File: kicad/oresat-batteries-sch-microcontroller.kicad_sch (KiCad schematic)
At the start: 28 parts, among them J2 SM14B-SHLS-TF, U20 TCAN330, U21 STM32F091C, X3 ECS-160-10-36Q-ES-TR

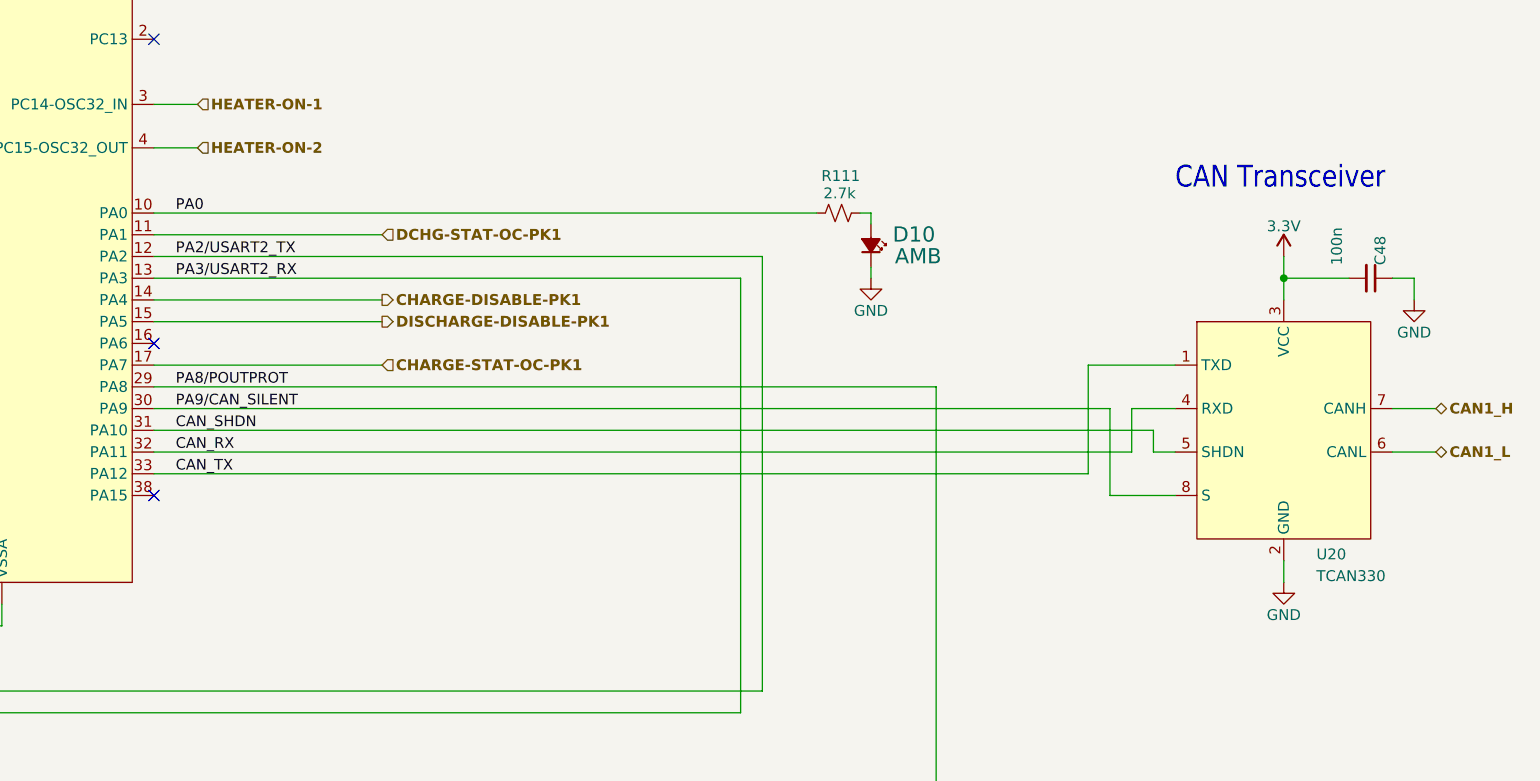
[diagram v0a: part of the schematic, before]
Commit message: Updated BOM, ready for polish and switch to MCXN
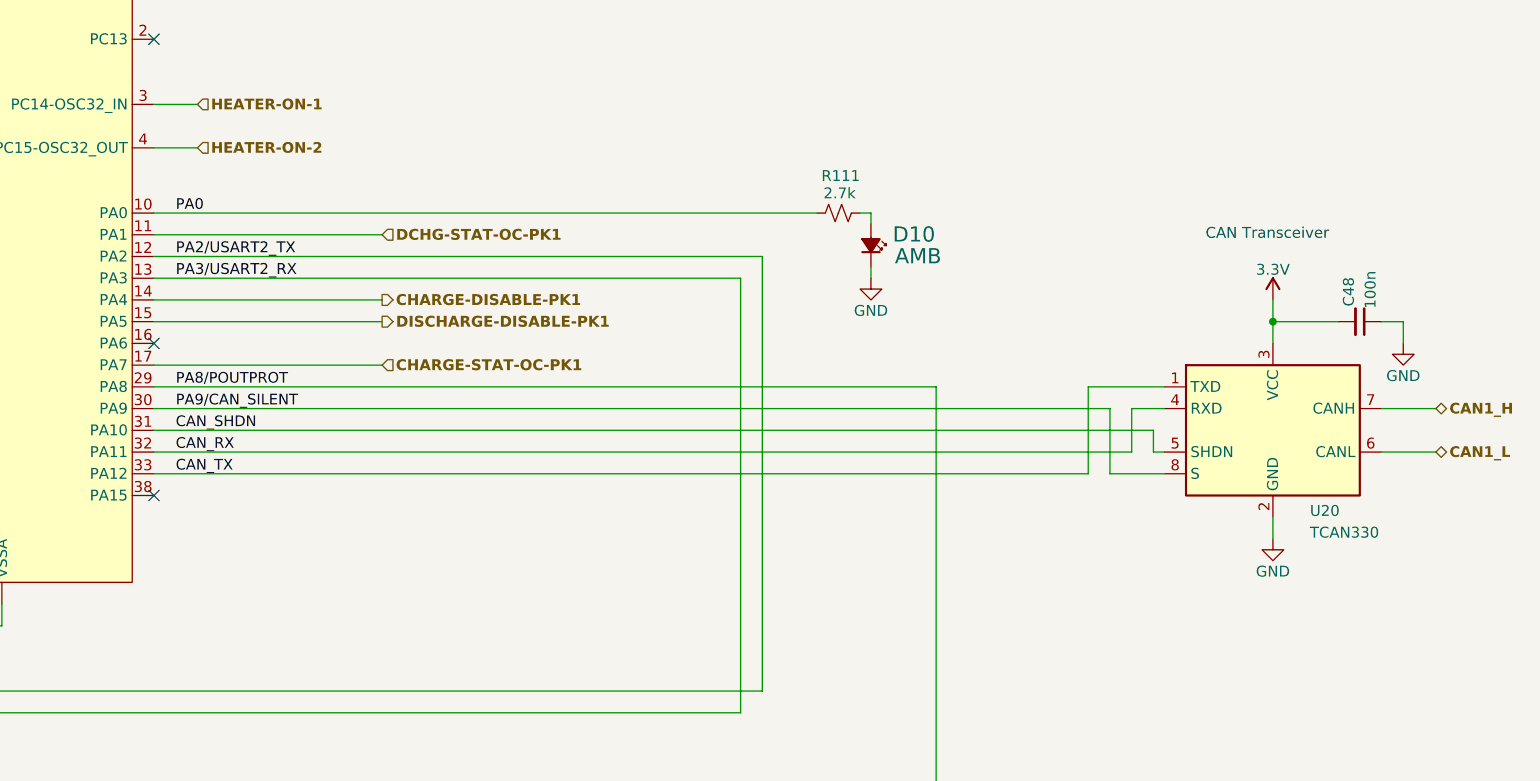
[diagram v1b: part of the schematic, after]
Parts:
- U20: footprint oresat-batteries:SOT23-8_TI-DCN -> Package_TO_SOT_SMD:SOT-23-8; symbol oresat-batteries-eagle-import:TCAN330 -> Interface_CAN_LIN:TCAN330
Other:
- moved on the sheet: C48, U20

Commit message: Not sure what changed from back in February, but committing anyway :)
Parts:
- C44, C45, C48, C49, C50: DIS Digi-Key -> DigiKey; DPN 399-1099-1-ND -> 399-6856-1-ND; MFR Samsung -> KEMET; MPN C0603C104M4RACTU -> C0603C104K5RACAUTO
- D10: DIS Digi-Key -> DigiKey; DPN 1830-1064-1-ND -> 732-150060AS75000CT-ND; MFR Inolux -> Wurth; MPN IN-S63AT5A -> 150060AS75000
- R110, R112: DIS Digi-Key -> DigiKey; DPN 311-10.0KHRCT-ND -> RMCF0603FT10K0CT-ND; MFR Yageo -> Stackpole Electronics; MPN RC0603FR-0710KL -> RMCF0603FT10K0
- R111: DIS Digi-Key -> DigiKey; DPN A129693CT-ND -> RMCF0603FT2K70CT-ND; MFR TE -> Stackpole Electronics; MPN CRGCQ0603F2K7 -> RMCF0603FT2K70
- R113, R114, R63, R64: DIS Digi-Key -> DigiKey; DPN RR08P4.7KDCT-ND -> RMCF0603FT4K70CT-ND; MFR TE Connectivity -> Stackpole Electronics; MPN RR0816P-472-D -> RMCF0603FT4K70
- R68, R72: DIS Digi-Key -> DigiKey; DPN RR08P4.7KDCT-ND -> RMCF0603FT10K0CT-ND; MFR TE Connectivity -> Stackpole Electronics; MPN RR0816P-472-D -> RMCF0603FT10K0
- U20: value TCAN330 -> TCAN330G; symbol Interface_CAN_LIN:TCAN330 -> Interface_CAN_LIN:TCAN330G; DIS Digi-Key -> DigiKey
- U21: DIS Digi-Key -> DigiKey; MPN STM32F091CBT6 -> STM32F091CCT7
- X3: DIS Digi-Key -> DigiKey

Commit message: Updated data, spiffed up the root page, renamed some STM specific OPD signals, synced SCH and BRD, fixed a bunch of DRC errors, NOW ready for MCXN import that will screw everything up.
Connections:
- net PA2/USART2_TX renamed MCU-UART-TX
- net PA3/USART2_RX renamed MCU-UART-RX
- net PB6/SCL renamed I2C1_SCL
- net PB7/SDA renamed I2C1_SDA
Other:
- note removed: "Emergency M0 bootstrapping over OPD I2C Address: 0b0111110x"
- note removed: "NOTE: PB6 and PB7 tied together via 2x 10k resistors @ MAX7310~{}"
- moved on the sheet: R110, R113, R114, TP21, TP22, TP78

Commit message: Added MCXN. Preliminary power layout, started removal of old symbols and footprints.
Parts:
- removed C46, C47: 20p, oresat-passives:0603-C-NOSILK, symbol Device:C_Small
- removed C49, C50: 100n, oresat-passives:0603-C-NOSILK, symbol Device:C_Small
- removed R110, R112, R68, R72: 10k, oresat-passives:0603-C-NOSILK, symbol Device:R_Small_US
- removed TP34, TP78, TP83: TEST-POINT-LARGE-SQUARE, oresat-misc:TestPoint-0.75mm-th, symbol oresat-misc:Test-Point-0.75mm-th
- removed U21: STM32F091C, oresat-batteries:STM32F091C, symbol oresat-batteries-eagle-import:STM32F091C
- removed X3: ECS-160-10-36Q-ES-TR, oresat-batteries:CRYSTAL_2.5X2, symbol oresat-batteries-eagle-import:CRYSTAL-WITH-GND
- added C38, C39: 4.7p, oresat-passives:0603-C-NOSILK, symbol Device:C_Small
- added C40, C52, C54, C55, C56, C57, C58, C59, C60: 100n, oresat-passives:0603-C-NOSILK, symbol Device:C_Small
- added C41: 1u, oresat-passives:0603-C-NOSILK, symbol Device:C_Small
- added C42: 2.2u, oresat-passives:0603-C-NOSILK, symbol Device:C_Small
- added C43: 22u, oresat-passives:0603-C-NOSILK, symbol Device:C_Small
- added C51, C53: 4.7u, oresat-passives:0603-C-NOSILK, symbol Device:C_Small
- added FB1: 120 ohm, oresat-passives:0805-B-NOSILK, symbol Device:FerriteBead_Small
- added L3: 1.5u, Inductor_SMD:L_0805_2012Metric, symbol Device:L_Small
- added R102: 1k, oresat-passives:0603-C-NOSILK, symbol Device:R_US
- added R108: 10k, oresat-passives:0603-C-NOSILK, symbol Device:R_Small_US
- added R115: 10k, oresat-passives:0603-C-NOSILK, symbol Device:R_US
- added TP113, TP6: Test-Point, oresat-misc:TestPoint-0.75mm-th, symbol oresat-misc:Test-Point-0.75mm-th
- added U7: MCXN947VKLT, oresat-ics:MCXN947KVLT-QFP50P1600X1600X160-101N, symbol oresat-ics:MCXN947VKLT
- added Y2: 24 MHz, Crystal:Crystal_SMD_2016-4Pin_2.0x1.6mm, symbol Device:Crystal_GND24_Small
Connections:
- net ALERTA-PK1: now also U7.22 (P4_0/ANA_0)
- net ALERTA-PK2: now also U7.28 (P4_6/ANA_6)
- net CHARGE-DISABLE-PK1: now also U7.25 (P4_3)
- net CHARGE-DISABLE-PK2: now also U7.36 (P4_13/ANA_14)
- net CHARGE-STAT-OC-PK1: now also U7.23 (P4_1/ANA_1)
- net CHARGE-STAT-OC-PK2: now also U7.29 (P4_7/ANA_7)
- net DCHG-STAT-OC-PK1: now also U7.24 (P4_2)
- net DCHG-STAT-OC-PK2: now also U7.35 (P4_12)
- net DISCHARGE-DISABLE-PK1: now also U7.26 (P4_4/ANA_4)
- net DISCHARGE-DISABLE-PK2: now also U7.37 (P4_15)
- net GND: now also C44.2, C45.2, C38.2, C39.2, C40.2, C41.2, C42.2, C43.2, C51.2, C52.2, C53.2, C54.2, C55.2, C56.2, C57.2, C58.2, C59.2, C60.2, U7.101 (EP), U7.32 (VREFL), U7.33 (VSS_P4), U7.52 (VSS_DCDC), Y2.2 (G), Y2.4 (G); no longer C44.1, C45.1
- net HEATER-ON-1: now also U7.27 (P4_5/ANA_5)
- net HEATER-ON-2: now also U7.38 (P4_16)
- net I2C1_SCL: now also U7.85 (P0_17)
- net I2C1_SDA: now also U7.84 (P0_16)
- net I2C2_SCL: now also R64.1, TP20.1, U7.93 (P1_1); no longer R63.1, TP19.1
- net I2C2_SDA: now also R63.1, TP19.1, U7.92 (P1_0); no longer R64.1, TP20.1
- net MCU-UART-RX: now also U7.1 (P1_8)
- net MCU-UART-TX: now also U7.2 (P1_9)
- net MOARPWR: now also U7.39 (P4_17/ANA_18)
- net SWCLK: now also U7.77 (P0_1)
- net SWDIO: now also U7.76 (P0_0)
- net at J2.8 (DEBUG-0): now also TP6.1
- net SWO: now reaches J2.13 (SWO)
- net SWO: now also U7.78 (P0_2)
- net 3.3V renamed +3.3V
- net +3.3V: now also C44.1, C45.1, C40.1, C51.1, C52.1, C54.1, C56.1, C57.1, C58.1, C59.1, FB1.1, R108.2, R115.2, U7.13 (VDD_LDO_CORE/VDD/VDD_P2), U7.34 (VDD_P4), U7.44 (VDD_USB), U7.47 (VDD_BAT), U7.54 (VDD_DCDC/VDD_LDO_SYS), U7.59 (VDD_P3), U7.66 (VDD_P3), U7.73 (VDD_P3), U7.83 (VDD), U7.96 (VDD); no longer C44.2, C45.2
- net CAN_RX: no longer names the net of U20.4 (RXD)
- net CAN_RX: now also U7.4 (P1_11)
- net CAN_SHDN: no longer names the net of U20.5 (SHDN)
- net CAN_TX: no longer names the net of U20.1 (TXD)
- net CAN_TX: now also U7.3 (P1_10)
- net NRESET renamed RESET
- net RESET: now also C60.1, R108.1, TP113.1, U7.9 (RESET_B)
- net PA0: no longer names the net of R111.2
- net PA0: now also U7.6 (P1_13)
- net PA9/CAN_SILENT: no longer names the net of U20.8 (S)
- new net: C38.1, U7.11 (P1_31), Y2.1
- new net: C39.1, U7.10 (P1_30), Y2.3
- new net: L3.2, U7.53 (DCDC_LX)
- new net 411-IOUT: R102.2
- new net P0_18: U7.86 (P0_18)
- new net P0_19: U7.87 (P0_19)
- new net P0_20: U7.88 (P0_20)
- new net P0_21: U7.89 (P0_21)
- new net P0_22: U7.90 (P0_22)
- new net P0_23: U7.91 (P0_23)
- new net P0_4: U7.80 (P0_4)
- new net P0_5: U7.81 (P0_5)
- new net P1_12: U7.5 (P1_12)
- new net P1_14: U7.7 (P1_14)
- new net P1_15: U7.8 (P1_15)
- new net P1_2: U7.94 (P1_2)
- new net P1_3: U7.95 (P1_3)
- new net P1_4: U7.97 (P1_4)
- new net P1_5: U7.98 (P1_5)
- new net P1_6: U7.99 (P1_6)
- new net P1_7: U7.100 (P1_7)
- new net P2_0: U7.14 (P2_0)
- new net P2_1: U7.15 (P2_1)
- new net P2_2: U7.16 (P2_2)
- new net P2_3: U7.17 (P2_3)
- new net P2_4: U7.18 (P2_4)
- new net P2_5: U7.19 (P2_5)
- new net P2_6: U7.20 (P2_6)
- new net P2_7: U7.21 (P2_7)
- new net P3_0: U7.75 (P3_0)
- new net P3_1: U7.74 (P3_1)
- new net P3_10: U7.68 (P3_10)
- new net P3_11: U7.67 (P3_11)
- new net P3_12: U7.65 (P3_12)
- new net P3_13: U7.64 (P3_13)
- new net P3_14: U7.63 (P3_14)
- new net P3_15: U7.62 (P3_15)
- new net P3_16: U7.61 (P3_16)
- new net P3_17: U7.60 (P3_17)
- new net P3_20: U7.57 (P3_20)
- new net P3_21: U7.56 (P3_21)
- new net P3_6: U7.72 (P3_6)
- new net P3_7: U7.71 (P3_7)
- new net P3_8: U7.70 (P3_8)
- new net P3_9: U7.69 (P3_9)
- new net P4_19: U7.40 (P4_19)
- new net P4_20: U7.41 (P4_20)
- new net P4_21: R102.1, U7.42 (P4_21/ANA_22)
- new net P4_23: U7.43 (P4_23)
- new net P5_0: U7.48 (P5_0)
- new net P5_1: U7.49 (P5_1)
- new net P5_2: U7.50 (P5_2)
- new net P5_3: U7.51 (P5_3)
- new net TDI : U7.79 (P0_3)
- new net VDD_ANA: C41.1, FB1.2, U7.30 (VDD_ANA), U7.31 (VREFH)
- new net VDD_CORE: C43.1, C53.1, C55.1, L3.1, U7.12 (VDD_CORE), U7.58 (VDD_CORE)
- new net VDD_SYS: C42.1, U7.55 (VDD_SYS)
- new net ~{ISPMODE}: R115.1, U7.82 (P0_6)
- no-connect marks 8 -> 55
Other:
- note added: "1.0 - 1.2 V depending on Active mode"
- note added: "24 MHz allows LPTMRs to work"
- note added: "4V"
- note added: "Note: Disable LDO_CORE in software for more power savings"
- note added: "OreSat Debug Connector"
- note added: "P0/P1"
- note added: "RX-TX cross on DEBUG board"
- note added: "VDD_BAT"
- note removed: "Battery CAN ID (SW pullups~{})"
- note removed: "Each VDD pin bypassed"
- note removed: "NRST pull-up built in"
- note removed: "Power/Current draw from OPD. Signal is analog voltage 0-1.2V"
- note removed: "Rx-Tx switch happens on programming board"
- note removed: "VBAT not bypassed becase not enough room instead tied into nearest bypass cap"
- moved on the sheet: C48, D10, J2, R111, R113, R114, R63, R64, TP19, TP20, TP21, TP22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

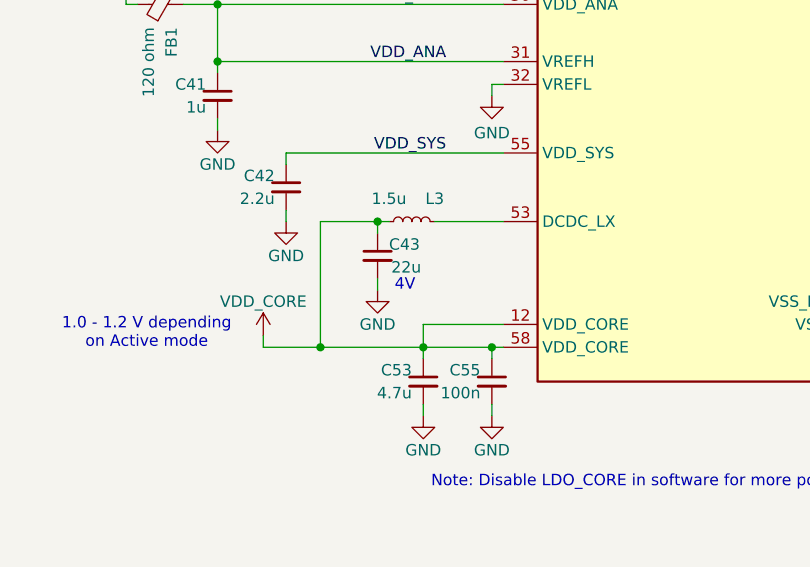
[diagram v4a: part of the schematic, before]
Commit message: Intermediary state on v4. Added one of two efuses.
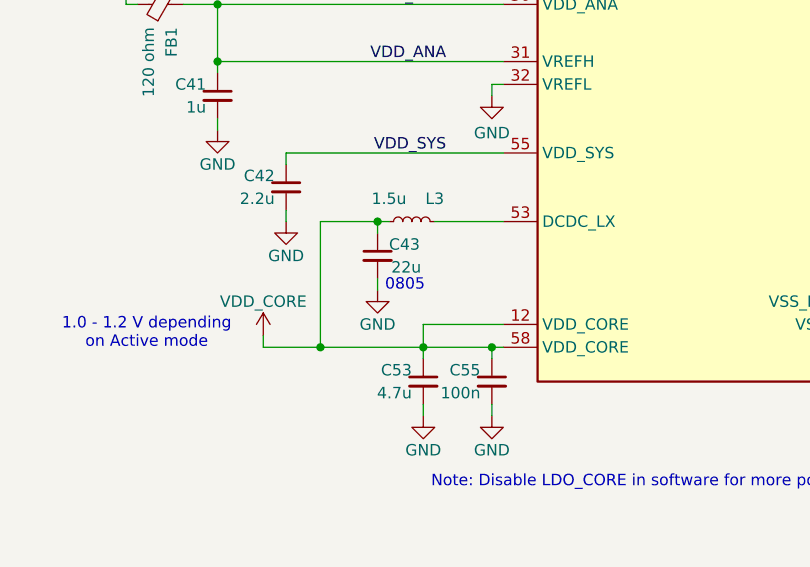
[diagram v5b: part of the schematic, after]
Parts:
- C43: footprint oresat-passives:0603-C-NOSILK -> oresat-passives:0805-C-NOSILK; DPN 478-KAM15CT70G226KTCT-ND -> 490-GRT21BC81C226ME13LCT-ND; MFR KYOCERA AVX -> Murata Electronics; MPN KAM15CT70G226KT -> GRT21BC81C226ME13L
- C51, C53: DPN 587-4332-1-ND -> 490-GRT188C71C475KE13DCT-ND; MFR Taiyo Yuden -> Murata Electronics; MPN EMK107BBJ475KAHT -> GRT188C71C475KE13D
- R102: DPN RMCF0603FT1K00CT-ND -> RMCF0603FT2K70CT-ND; MFR Stackpole Electronics Inc -> Stackpole Electronics
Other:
- note added: "0805"
- note removed: "4V"
